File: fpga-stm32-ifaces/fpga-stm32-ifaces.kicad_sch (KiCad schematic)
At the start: 2 parts, among them U1 STM32H735-UFBGA176-25, U2 XC7S25-1FTGB196

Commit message: Finished initial schematic of fpga-stm32-ifaces board, waiting for sch review
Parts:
- added J11: XILINX_JTAG, symbol xilinx-azonenberg:XILINX_JTAG
- added J12: CONN_01X03, azonenberg_pcb:CONN_HEADER_2.54MM_1x3, symbol conn:CONN_01X03
- added R78, R79: 33, symbol device:R
- added R85: 10K, azonenberg_pcb:EIA_0402_RES_NOSILK, symbol device:R
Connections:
- net MCU_BOOT0: now reaches U1.C5 (BOOT0)
- net MCU_BOOT0: now also R85.1
- net 3V3: now reaches U1.D4 (PDR_ON)
- net 3V3: now also U1.M3 (VREF+), U2.M7 (M0_0), U2.N7 (CFGBVS_0), J11.2 (Vccaux), J12.1 (P1)
- net MCU_RST_N: now reaches U1.L1 (NRST)
- net GND: now reaches U1.L4 (VREF-)
- net GND: now also U2.G7 (VREFN_0), U2.G8 (VP_0), U2.H7 (VN_0), U2.H8 (VREFP_0), U2.J7 (DXN_0), U2.J8 (DXP_0), U2.M8 (M1_0), U2.M9 (M2_0), J11.11 (Vss), J11.3 (Vss), J11.5 (Vss), J11.7 (Vss), J11.9 (Vss), J12.3 (P3)
- net FPGA_TCK: now reaches U2.A7 (TCK_0)
- net FPGA_TCK: now also J11.6 (TCK)
- net at U2.A8 (CCLK_0): now also R78.1
- net FPGA_RST_N: now reaches U2.L7 (PROGRAM_B_0)
- net FPGA_TMS: now reaches U2.M6 (TMS_0)
- net FPGA_TMS: now also J11.4 (TMS)
- net at U2.P6 (TDO_0): now also R79.2
- net FPGA_TDI: now reaches U2.P7 (TDI_0)
- net FPGA_TDI: now also J11.10 (TDI_OUT)
- net FPGA_INIT: now reaches U2.P8 (INIT_B_0)
- net FPGA_DONE: now reaches U2.P9 (DONE_0)
- new net: J12.2 (P2), R85.2
- new net FPGA_FLASH_SCK: R78.2
- new net FPGA_TDO: J11.8 (TDO_IN), R79.1
- no-connect marks 0 -> 2
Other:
- sheet Ethernet ports: added 1V2, 3V3, FPGA_FLASH_SCK, GND; removed none
- sheet MCU ports: added 3V3, FPGA_DONE, GND, MCU_RST_N, SUPER_SPI_CS_N, SUPER_SPI_MISO, SUPER_SPI_MOSI, SUPER_SPI_SCK; removed none
- sheet Power supply ports: added 12V0, 1V0, 1V2, 1V8, 3V3, 3V3_SB, FPGA_DONE, FPGA_INIT, FPGA_RST_N, GND, MCU_RST_N, SUPER_SPI_CS_N, SUPER_SPI_MISO, SUPER_SPI_MOSI, SUPER_SPI_SCK; removed none
- sheet Power support ports: added 1V0, 1V8, 3V3, 3V3_SB, GND; removed none
- moved on the sheet: U1K

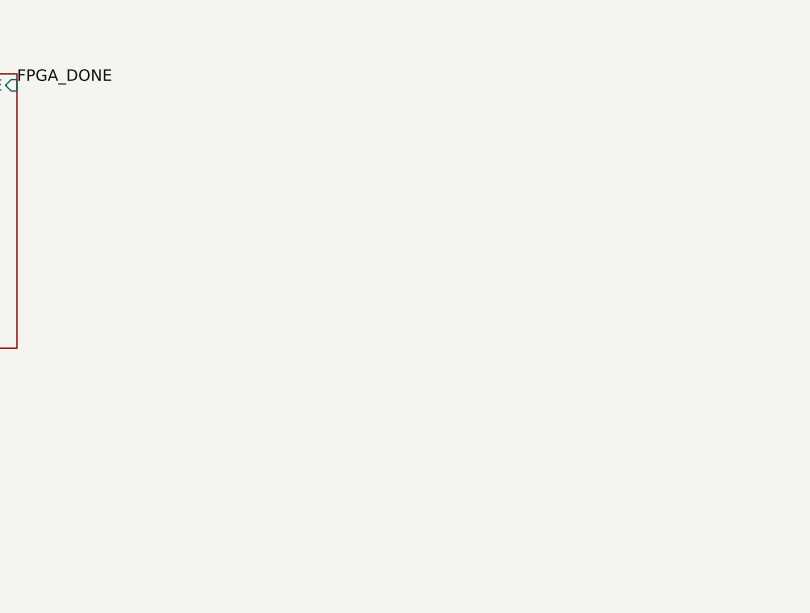
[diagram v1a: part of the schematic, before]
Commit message: Continued initial layout of fpga-stm32-ifaces
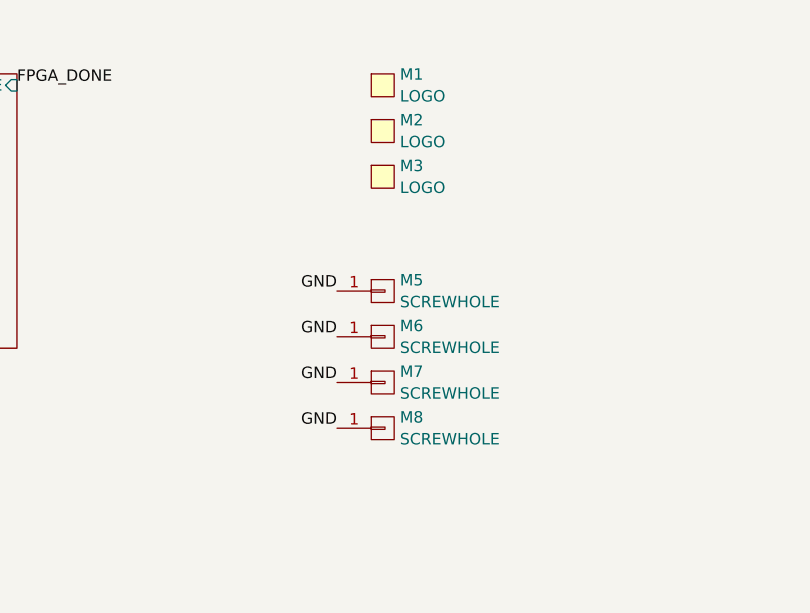
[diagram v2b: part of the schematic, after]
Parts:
- added M1: LOGO, azonenberg_pcb:LONGTHING-1200DPI, symbol special-azonenberg:MECHANICAL
- added M2: LOGO, w_logo:Logo_silk_OSHW_6x6mm, symbol special-azonenberg:MECHANICAL
- added M3: LOGO, w_logo:Logo_silk_WEEE_3.4x5mm, symbol special-azonenberg:MECHANICAL
- added M5, M6, M7, M8: SCREWHOLE, azonenberg_pcb:MECHANICAL_CLEARANCEHOLE_4_40, symbol conn:CONN_01X01
- J11: footprint (none) -> azonenberg_pcb:XILINX_JTAG_PTH_MOLEX_0878311420
- R78, R79: footprint (none) -> azonenberg_pcb:EIA_0402_RES_NOSILK
- U1: footprint (none) -> azonenberg_pcb:BGA_201_10x10_DEPOP_0.65MM_OSHPARK
- U2: footprint (none) -> azonenberg_pcb:BGA_196_15x15_FULLARRAY_1MM_FTGB196
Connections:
- net GND: now also M5.1 (P1), M6.1 (P1), M7.1 (P1), M8.1 (P1)
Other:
- company: (none) -> Antikernel Labs
- title: (none) -> FPGA - STM32 Interface Test
